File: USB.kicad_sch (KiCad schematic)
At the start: 5 parts, among them J2 USB-C_GCT_USB4105-GF-A, Q1 PJE138K, U1 TPD4E05U06QDQARQ1

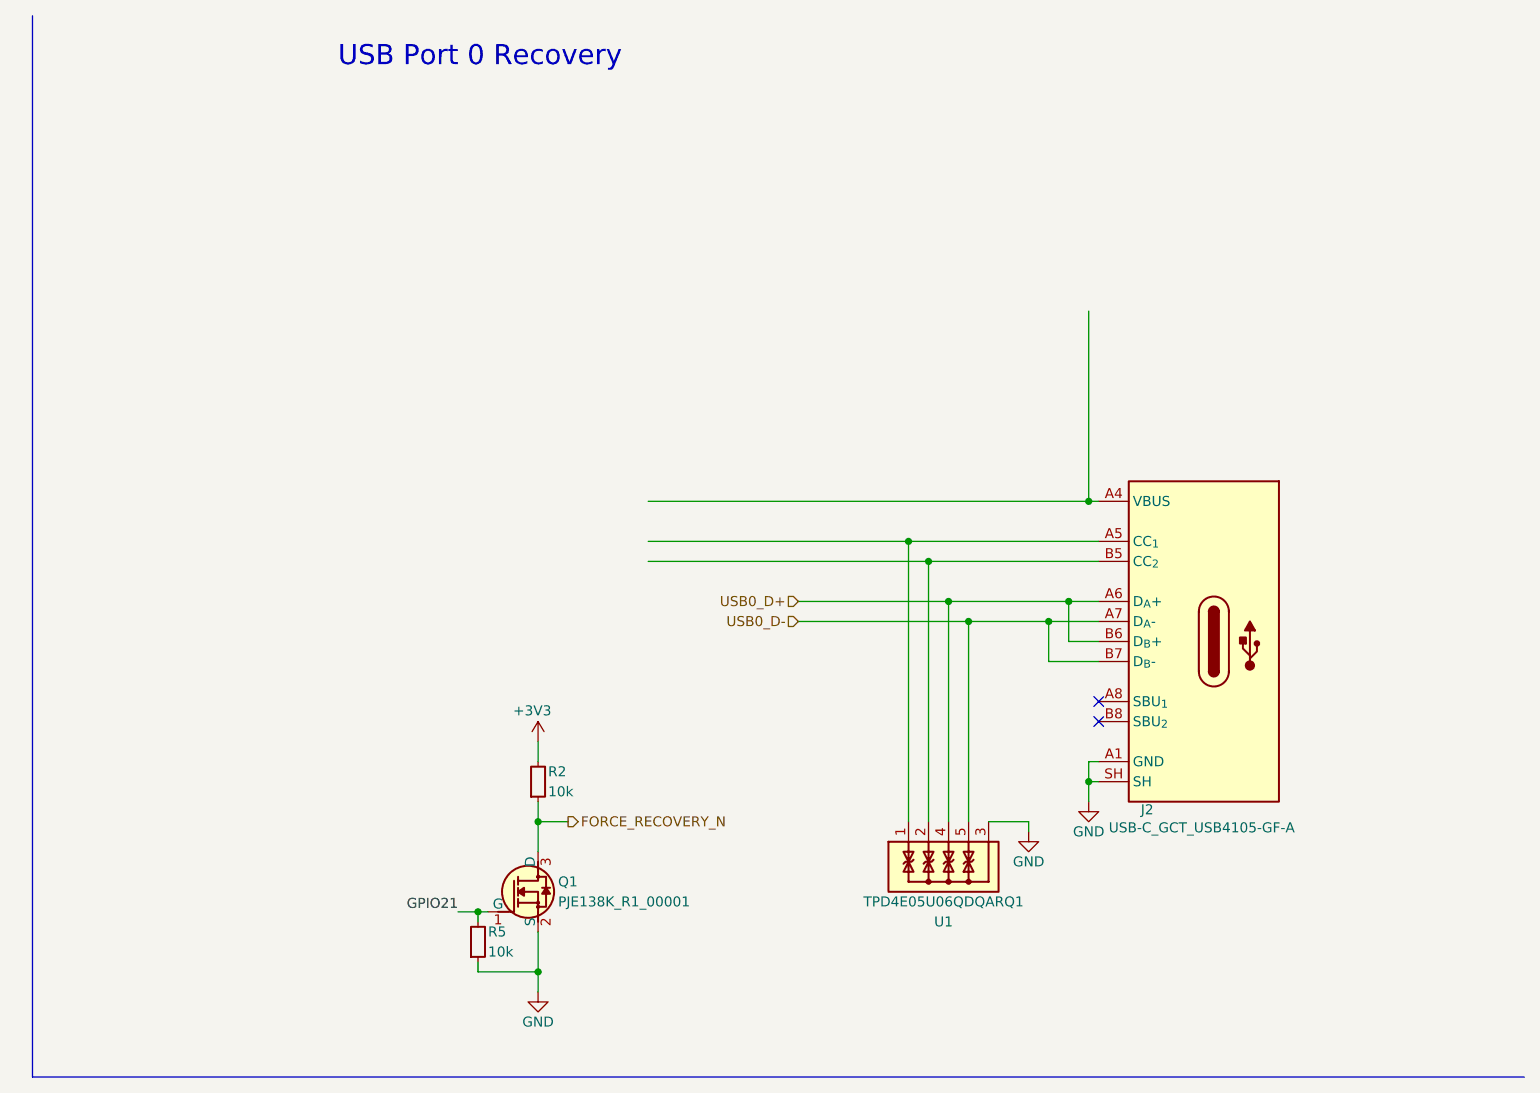
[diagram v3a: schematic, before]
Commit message: [#82055] Add interface controller for USBC0
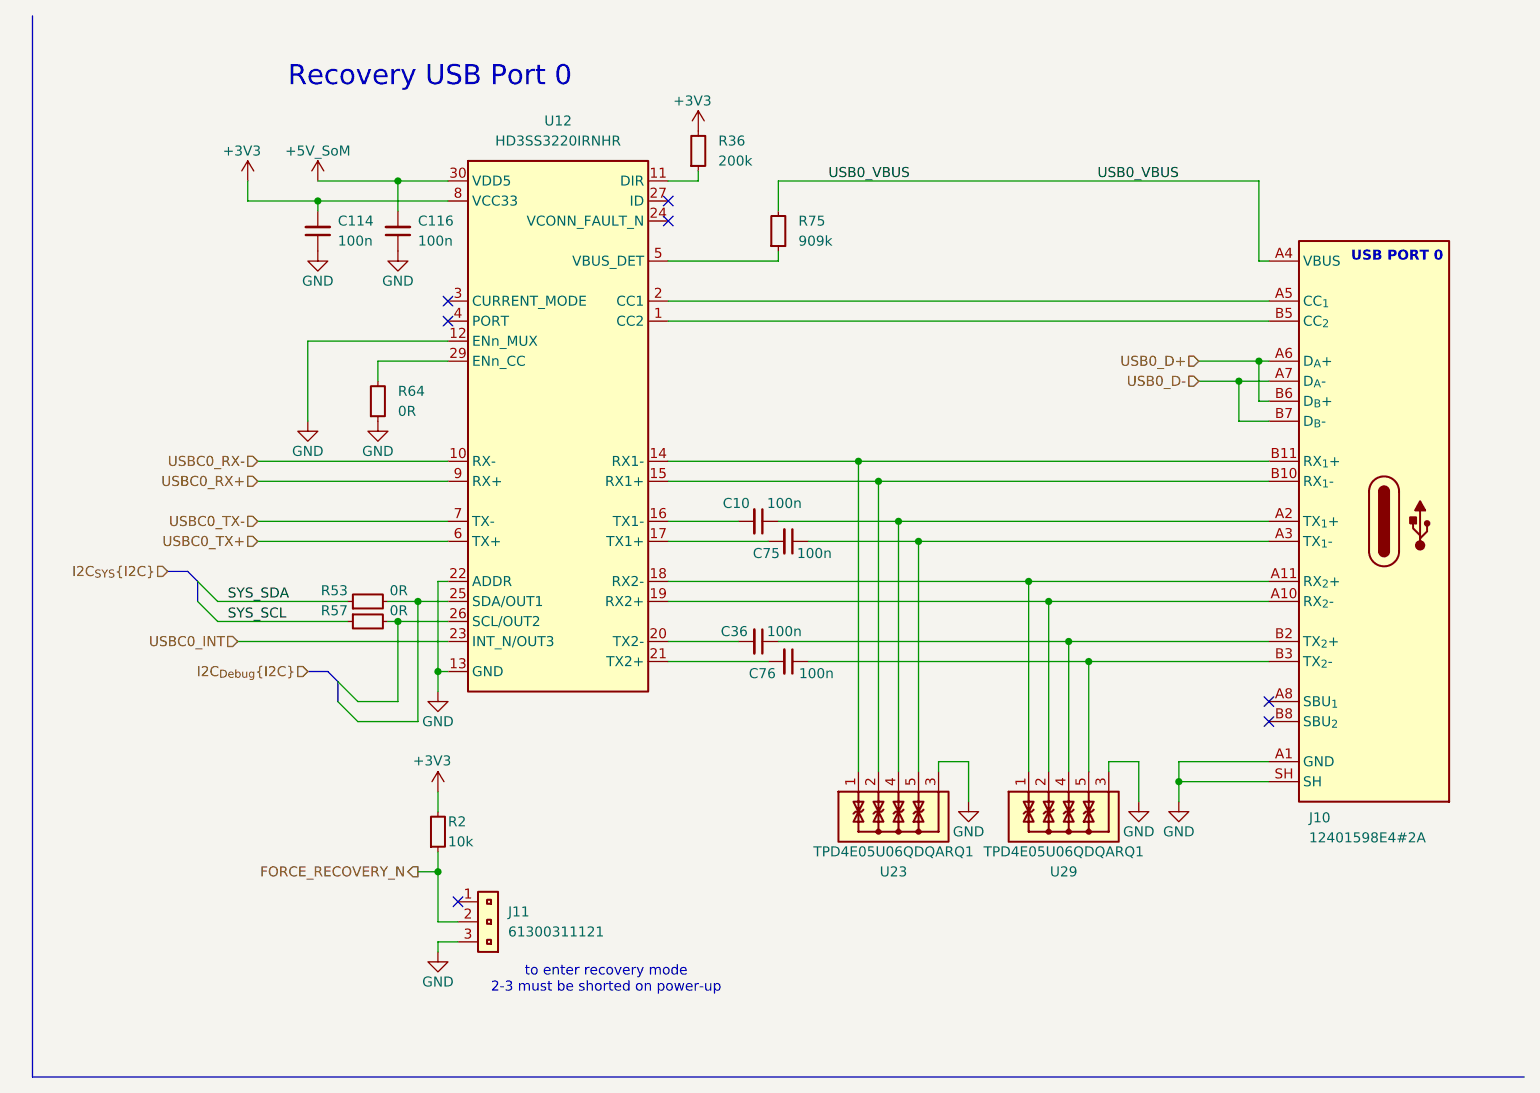
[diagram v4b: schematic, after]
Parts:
- removed J2: USB-C_GCT_USB4105-GF-A, antmicro-footprints:USB-C_Receptacle_GCT_USB4105-GF-A, symbol antmicroUSBConnectors:USB-C_GCT_USB4105-GF-A
- removed Q1: PJE138K, antmicro-footprints:SOT-523, symbol antmicroTransistorsFETsMOSFETsSingle:PJE138K
- removed R5: R_10k_0402, antmicro-footprints:R_0402_1005Metric, symbol antmicroResistors0402:R_10k_0402
- removed U1: TPD4E05U06QDQARQ1, antmicro-footprints:USON-10_2.5x1mm_P0.5mm, symbol antmicroTVSDiodes:TPD4E05U06QDQARQ1
- added C10, C36, C75, C76: C_100n_0201, antmicro-footprints:C_0201, symbol antmicroCapacitorsmisc:C_100n_0201
- added C114, C116: C_100n_50V_X8L_0402, antmicro-footprints:C_0402_1005Metric, symbol antmicroCapacitors0402:C_100n_50V_X8L_0402
- added J10: USB-C_Amphenol_12401598E4, antmicro-footprints:USB-C_Receptacle_Amphenol_12401598E4, symbol antmicroUSBConnectors:USB-C_Amphenol_12401598E4
- added J11: PinHeader_1x3_P2.54mm_Drill1.1mm, antmicro-footprints:PinHeader_1x3_P2.54mm_Drill1.1mm, symbol antmicroGenericPinHeaders:PinHeader_1x3_P2.54mm_Drill1.1mm
- added R36: R_200k_0402, antmicro-footprints:R_0402_1005Metric, symbol antmicroResistors0402:R_200k_0402
- added R53, R57, R64: R_0R_0402, antmicro-footprints:R_0402_1005Metric, symbol antmicroResistors0402:R_0R_0402
- added R75: R_909k_0402, antmicro-footprints:R_0402_1005Metric, symbol antmicroResistors0402:R_909k_0402
- added U12: HD3SS3220IRNHR, antmicro-footprints:WQFN-30-1EP_4.6x2.6mm_P0.4mm, symbol antmicroInterfaceControllers:HD3SS3220IRNHR
- added U23, U29: TPD4E05U06QDQARQ1, antmicro-footprints:USON-10_2.5x1mm_P0.5mm, symbol antmicroTVSDiodes:TPD4E05U06QDQARQ1
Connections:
- net +3V3: now also C114.2, R36.2, U12.8 (VCC33)
- net FORCE_RECOVERY_N: now also J11.2
- net GND: now also C114.1, C116.1, J10.A1 (GND), J10.A12 (GND), J10.B1 (GND), J10.B12 (GND), J10.SH, J11.3, R64.1, U12.12 (ENn_MUX), U12.13 (GND), U12.22 (ADDR), U12.28 (GND), U12.31 (GND), U23.3, U23.8, U29.3, U29.8
- net USB0_D+: now also J10.A6 (D_{A}+), J10.B6 (D_{B}+)
- net USB0_D-: now also J10.A7 (D_{A}-), J10.B7 (D_{B}-)
- new net: R64.2, U12.29 (ENn_CC)
- new net: C10.1, J10.A2 (TX_{1}+), U23.4, U23.7
- new net: C10.2, U12.16 (TX1-)
- new net: J10.B11 (RX_{1}+), U12.14 (RX1-), U23.1, U23.10
- new net: J10.B10 (RX_{1}-), U12.15 (RX1+), U23.2, U23.9
- new net: C75.1, J10.A3 (TX_{1}-), U23.5, U23.6
- new net: J10.B5 (CC_{2}), U12.1 (CC2)
- new net: R36.1, U12.11 (DIR)
- new net: C75.2, U12.17 (TX1+)
- new net: J10.A11 (RX_{2}+), U12.18 (RX2-), U29.1, U29.10
- new net: J10.A10 (RX_{2}-), U12.19 (RX2+), U29.2, U29.9
- new net: J10.A5 (CC_{1}), U12.2 (CC1)
- new net: C36.2, U12.20 (TX2-)
- new net: C76.2, U12.21 (TX2+)
- new net: R53.2, U12.25 (SDA/OUT1)
- new net: R57.2, U12.26 (SCL/OUT2)
- new net: R75.1, U12.5 (VBUS_DET)
- new net: C36.1, J10.B2 (TX_{2}+), U29.4, U29.7
- new net: C76.1, J10.B3 (TX_{2}-), U29.5, U29.6
- new net +5V_SoM: C116.2, U12.30 (VDD5)
- new net SYS_SCL: R57.1
- new net SYS_SDA: R53.1
- new net USB0_VBUS: J10.A4 (VBUS), J10.A9 (VBUS), J10.B4 (VBUS), J10.B9 (VBUS), R75.2
- new net USBC0_INT: U12.23 (INT_N/OUT3)
- new net USBC0_RX+: U12.9 (RX+)
- new net USBC0_RX-: U12.10 (RX-)
- new net USBC0_TX+: U12.6 (TX+)
- new net USBC0_TX-: U12.7 (TX-)
- no-connect marks 2 -> 7
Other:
- note added: "Recovery USB Port 0"
- note added: "USB PORT 0"
- note added: "to enter recovery mode 2-3 must be shorted on power-up"
- note removed: "USB Port 0 Recovery"
- moved on the sheet: R2

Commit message: [#82055] Add port 3,4 connect to hub
[#82055] Change I2C bus

[#82055] Cleanup pin assigment

[#82055] Cleanup
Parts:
- added C172, C173, C174, C175, C176, C177, C178, C179, C183, C184, C185, C186, C187, C188, C189, C190: C_100n_16V_X7R_0402, antmicro-footprints:C_0402_1005Metric, symbol antmicroCapacitors0402:C_100n_16V_X7R_0402
- added C180: C_100n_50V_X8L_0402, antmicro-footprints:C_0402_1005Metric, symbol antmicroCapacitors0402:C_100n_50V_X8L_0402
- added C181, C182: C_10u_0402, antmicro-footprints:C_0402_1005Metric, symbol antmicroCapacitors0402:C_10u_0402
- added C191, C193, C194, C195, C196, C197, C198, C199: C_100n_0201, antmicro-footprints:C_0201, symbol antmicroCapacitorsmisc:C_100n_0201
- added C192: C_100n_0402, antmicro-footprints:C_0402_1005Metric, symbol antmicroCapacitors0402:C_100n_0402
- added C200, C201, C202, C203, C204, C205, C206, C207: C_330n_0402, antmicro-footprints:C_0402_1005Metric, symbol antmicroCapacitors0402:C_330n_0402
- added D41: RB521S30T1G, antmicro-footprints:SOD-523, symbol antmicroDiodesRectifiersSingle:RB521S30T1G
- added J15, J16: USB-C_Amphenol_12401598E4, antmicro-footprints:USB-C_Receptacle_Amphenol_12401598E4, symbol antmicroUSBConnectors:USB-C_Amphenol_12401598E4
- added R226, R227, R228, R229, R238, R241, R242, R243, R244, R245, R246: R_10k_0402, antmicro-footprints:R_0402_1005Metric, symbol antmicroResistors0402:R_10k_0402
- added R230: R_12k_0402, antmicro-footprints:R_0402_1005Metric, symbol antmicroResistors0402:R_12k_0402
- added R231, R234, R235: R_200k_0402, antmicro-footprints:R_0402_1005Metric, symbol antmicroResistors0402:R_200k_0402
- added R232: R_20k_0402, antmicro-footprints:R_0402_1005Metric, symbol antmicroResistors0402:R_20k_0402
- added R233: R_49k9_0402, antmicro-footprints:R_0402_1005Metric, symbol antmicroResistors0402:R_49k9_0402
- added R237: R_4x0R_0201_array, antmicro-footprints:R_Array_4x0201_Panasonic_EXB18V, symbol antmicroResistorNetworksArrays:R_4x0R_0201_array
- added R239, R240: R_0R_0402, antmicro-footprints:R_0402_1005Metric, symbol antmicroResistors0402:R_0R_0402
- added U1: USB7252C, antmicro-footprints:VQFN-100-1EP_12x12x0.85mm_P0.4mm, symbol antmicroInterfaceControllers:USB7252C
- added U46: AP7366_SOT, antmicro-footprints:SOT-23-5, symbol antmicroPMICVoltageRegulatorsLinear:AP7366_SOT
- added U47, U49, U50, U51: TPD4E05U06QDQARQ1, antmicro-footprints:USON-10_2.5x1mm_P0.5mm, symbol antmicroTVSDiodes:TPD4E05U06QDQARQ1
- added U48: W25Q80DV_USON, antmicro-footprints:USON-8_2x3mm_P0.5mm, symbol antmicroMemory:W25Q80DV_USON
- added Y3: Oscillator_25MHz_ESC_2016MV, antmicro-footprints:Oscillator_SMD_ECS_2016MV_2x1.6x0.85mm, symbol antmicroOscillators:Oscillator_25MHz_ESC_2016MV
- renumbered C114 to C1, C116 to C2, C10 to C3, C36 to C4, C75 to C5, C76 to C6, J11 to J1, J10 to J2, R53 to R1, R57 to R2, R64 to R3, R2 to R4, R36 to R5, R75 to R6, U12 to U2, U23 to U3, U29 to U4
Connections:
- net +3V3: now also C172.2, C173.2, C174.2, C175.2, C176.2, C177.2, C178.2, C179.2, C180.2, C181.2, D41.2 (A), R226.1, R227.1, R228.1, R229.1, R238.2, R241.2, R246.1, U1.26 (VDD33), U1.42 (VDD33), U1.53 (VDD33), U1.62 (VDD33), U1.67 (VDD33), U1.79 (VDD33), U1.88 (VDD33), U1.99 (VDD33), U46.1 (IN), U46.3 (EN), Y3.1 (EN), Y3.4 (VDD)
- net GND: now also C172.1, C173.1, C174.1, C175.1, C176.1, C177.1, C178.1, C179.1, C180.1, C181.1, C182.1, C183.1, C184.1, C185.1, C186.1, C187.1, C188.1, C189.1, C190.1, C192.1, J15.A1 (GND), J15.A12 (GND), J15.B1 (GND), J15.B12 (GND), J15.SH, J16.A1 (GND), J16.A12 (GND), J16.B1 (GND), J16.B12 (GND), J16.SH, R230.1, R231.1, R233.1, R234.1, R235.1, R242.2, R243.2, R244.2, R245.2, U1.101 (VSS), U1.24 (TESTEN), U46.2 (GND), U47.3, U47.8, U48.4 (VSS), U49.3, U49.8, U50.3, U50.8, U51.3, U51.8, Y3.2 (GND)
- new net: C206.2, J15.B10 (RX_{1}-)
- new net: C205.2, J15.A11 (RX_{2}+)
- new net: R238.1, U1.4 (DP1_VBUS_MON)
- new net: C182.2, C183.2, C184.2, C185.2, C186.2, C187.2, C188.2, C189.2, C190.2, R232.2, U1.18 (VCORE), U1.25 (VCORE), U1.33 (VCORE), U1.39 (VCORE), U1.55 (VCORE), U1.78 (VCORE), U1.85 (VCORE), U1.9 (VCORE), U1.93 (VCORE), U46.5 (OUT)
- new net: C203.2, J16.A10 (RX_{2}-), U49.2, U49.9
- new net: R226.2, U1.1 (RESET_N)
- new net: R230.2, U1.100 (RBIAS)
- new net: J16.A5 (CC_{1}), U1.12 (DP1_CC1)
- new net: J16.B5 (CC_{2}), U1.13 (DP1_CC2)
- new net: R234.2, U1.21 (CFG_STRAP1)
- new net: R235.2, U1.22 (CFG_STRAP2)
- new net: R231.2, U1.23 (CFG_STRAP3)
- new net: J15.A5 (CC_{1}), U1.27 (DP2_CC1)
- new net: J15.B5 (CC_{2}), U1.28 (DP2_CC2)
- new net: R241.1, U1.36 (DP2_VBUS_MON)
- new net: R228.2, U1.63 (TEST1)
- new net: R227.2, U1.64 (TEST2)
- new net: R229.2, U1.65 (TEST3)
- new net: R246.2, U1.80 (VBUS_MON_UP)
- new net: U1.98 (XTALI), Y3.3 (OUT)
- new net: C200.2, J16.B11 (RX_{1}+), U47.1, U47.10
- new net: C191.1, J16.A2 (TX_{1}+), U47.4, U47.7
- new net: C193.1, J16.B2 (TX_{2}+), U49.4, U49.7
- new net: C199.1, J15.B3 (TX_{2}-), U51.5, U51.6
- new net: R232.1, R233.2, U46.4 (ADJ)
- new net: C198.1, J15.A3 (TX_{1}-), U50.5, U50.6
- new net: C202.2, J16.A11 (RX_{2}+), U49.1, U49.10
- new net: C194.1, J16.A3 (TX_{1}-), U47.5, U47.6
- new net: C196.1, J15.A2 (TX_{1}+), U50.4, U50.7
- new net: R237.6 (R3.2), U48.3 (~{WP}/IO2)
- new net: R237.5 (R4.2), U48.7 (~{HOLD}/IO3)
- new net: C207.2, J15.A10 (RX_{2}-)
- new net: J15.A4 (VBUS), J15.A9 (VBUS), J15.B4 (VBUS), J15.B9 (VBUS)
- new net: C204.2, J15.B11 (RX_{1}+)
- new net: C197.1, J15.B2 (TX_{2}+), U51.4, U51.7
- new net: C195.1, J16.B3 (TX_{2}-), U49.5, U49.6
- new net: J16.A4 (VBUS), J16.A9 (VBUS), J16.B4 (VBUS), J16.B9 (VBUS)
- new net: C201.2, J16.B10 (RX_{1}-), U47.2, U47.9
- new net DEBUG_SCL: U1.75 (PF26)
- new net DEBUG_SDA: U1.66 (PF19)
- new net FLASH_PWR: C192.2, D41.1 (C), U48.8 (VCC)
- new net HUB_MISO: R237.7 (R2.2), U48.2 (SO/IO1)
- new net HUB_MOSI: R237.8 (R1.2), U48.5 (SI/IO0)
- new net HUB_SCLK: R239.2, U48.6 (SCLK)
- new net HUB_SPI_CE_N: R240.1, U1.69 (SPI_CE_N)
- new net HUB_SPI_CLK: R239.1, U1.68 (SPI_CLK)
- new net HUB_SPI_D0: R237.1 (R1.1), U1.70 (SPI_D0)
- new net HUB_SPI_D1: R237.2 (R2.1), U1.71 (SPI_D1)
- new net HUB_SPI_D2: R237.3 (R3.1), U1.72 (SPI_D2)
- new net HUB_SPI_D3: R237.4 (R4.1), U1.73 (SPI_D3)
- new net PRT_CTL1: R243.1, U1.60 (PF17)
- new net PRT_CTL2: R242.1, U1.58 (PF15)
- new net PRT_CTL3: R245.1, U1.56 (PF13)
- new net PRT_CTL4: R244.1, U1.59 (PF16)
- new net USB3_D+: J16.A6 (D_{A}+), J16.B6 (D_{B}+)
- new net USB3_D-: J16.A7 (D_{A}-), J16.B7 (D_{B}-)
- new net USB4_D+: J15.A6 (D_{A}+), J15.B6 (D_{B}+), U1.29 (USB2DN_DP2)
- new net USB4_D-: J15.A7 (D_{A}-), J15.B7 (D_{B}-), U1.30 (USB2DN_DM2)
- new net USBC3_RX_{1}+: C200.1, U1.10 (USB3DN_RXDP1A)
- new net USBC3_RX_{1}-: C201.1, U1.11 (USB3DN_RXDM1A)
- new net USBC3_RX_{2}+: C202.1, U1.20 (USB3DN_RXDP1B)
- new net USBC3_RX_{2}-: C203.1, U1.19 (USB3DN_RXDP1B)
- new net USBC3_TX_{1}+: C191.2, U1.7 (USB3DN_TXDP1A)
- new net USBC3_TX_{1}-: C194.2, U1.8 (USB3DN_TXDM1A)
- new net USBC3_TX_{2}+: C193.2, U1.16 (USB3DN_TXDP1B)
- new net USBC3_TX_{2}-: C195.2, U1.17 (USB3DN_TXDM1B)
- new net USBC4_RX_{1}+: C204.1, U1.34 (USB3DN_RXDP2A), U50.1, U50.10
- new net USBC4_RX_{1}-: C206.1, U1.35 (USB3DN_RXDM2A), U50.2, U50.9
- new net USBC4_RX_{2}+: C205.1, U1.40 (USB3DN_RXDP2B), U51.1, U51.10
- new net USBC4_RX_{2}-: C207.1, U1.41 (USB3DN_RXDM2B), U51.2, U51.9
- new net USBC4_TX_{1}+: C196.2, U1.31 (USB3DN_TXDP2A)
- new net USBC4_TX_{1}-: C198.2, U1.32 (USB3DN_TXDM2A)
- new net USBC4_TX_{2}+: C197.2, U1.37 (USB3DN_TXDP2B)
- new net USBC4_TX_{2}-: C199.2, U1.38 (USB3DN_TXDM2B)
- new net USBHUB_DM: U1.90 (USB2UP_DM)
- new net USBHUB_DP: U1.89 (USB2UP_DP)
- new net USBHUB_RXDM: U1.95 (USB3UP_RXDM)
- new net USBHUB_RXDP: U1.94 (USB3UP_RXDP)
- new net USBHUB_TXDM: U1.92 (USB3UP_TXDM)
- new net USBHUB_TXDP: U1.91 (USB3UP_TXDP)
- new net ~{HUB_CS}: R240.2, U48.1 (~{CS})
- no-connect marks 7 -> 41
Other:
- note added: "1.12V [1.1V ... 1.14V]"
- note added: "USB PORT 3"
- note added: "USB PORT 4"
- note added: "USB hub"
- moved on the sheet: C1, C2, C3, C4, C5, C6, J1, J2, R1, R2, R3, R4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
